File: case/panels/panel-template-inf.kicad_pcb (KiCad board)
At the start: 2 copper layers, 100 x 128.5 mm, 4 parts

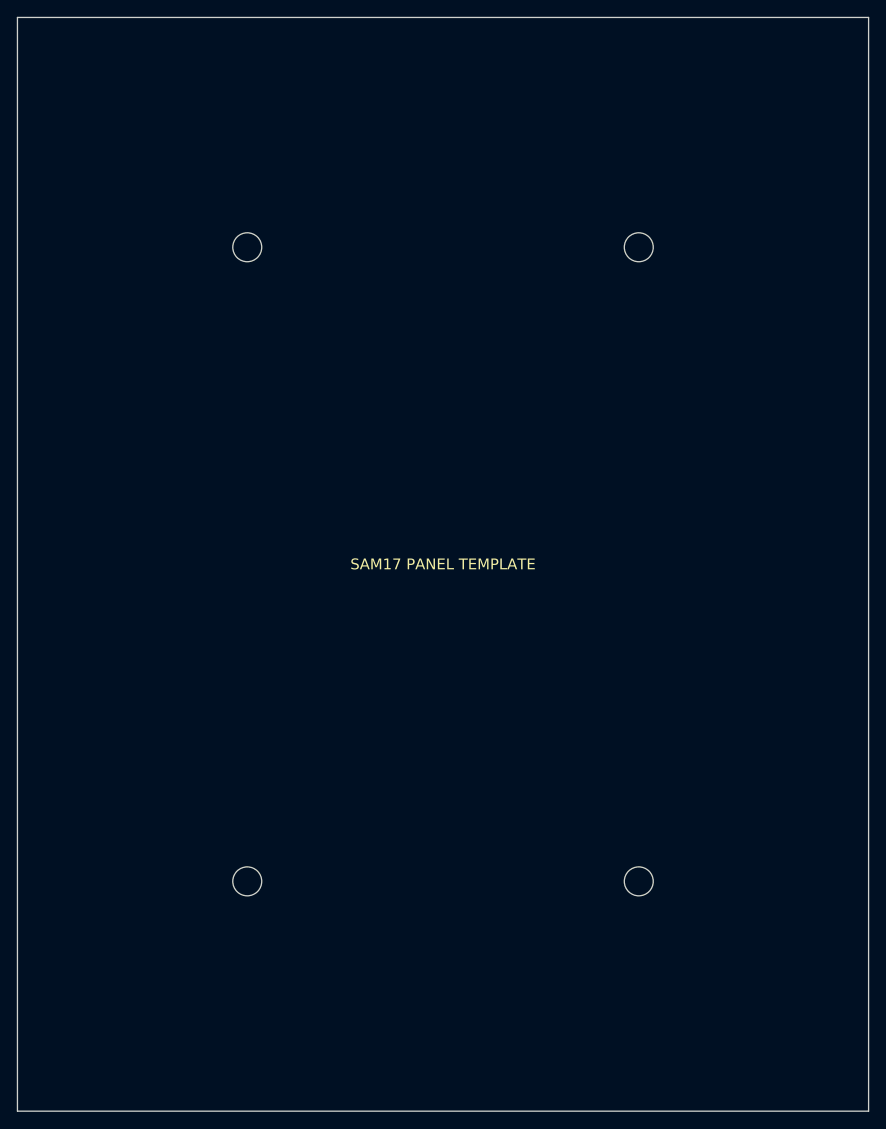
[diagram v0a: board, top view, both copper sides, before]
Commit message: Case: cara y panel dejan de ser el mismo numero, y EUROrack pasa a verde
La puerta de EUROrack estaba roja porque `alto_panel_inf` hacia dos trabajos
a la vez: era el tramo del perfil del costado Y el alto de la PCB. Con los
dos valiendo 128.5 y los railes a inset 27 de cada punta, los railes
quedaban a 74.5 mm y un modulo 3U no atornillaba.

Se separan:

  alto_cara_*   el tramo del perfil. Dibuja la silueta y sujeta los railes.
  alto_panel_*  la PCB de aluminio. Es lo unico que ve el fabricante.

En el piso de arriba coinciden (el panel cubre la cara entera; hay un assert
que lo exige). En el de abajo ya no pueden, y la cara se dimensiona DESDE el
estandar en vez de al reves:

  alto_cara_inf = sep_railes_inf + inset_tornillo + inset_valle
                = 122.5 + 27 + 15 = 164.5

Los dos insets de esa cara son asimetricos a proposito. Por delante la punta
redondeada vacia alto_frontal/2 = 15 mm de acrilico, asi que el riel no puede
empezar antes de 15 + rail/2 + 2 = 27. Por el valle el vertice lleva
radio_pico = 5 y su tangente mide 2.60, asi que con 15 basta. Forzar la
simetria costaba 12 mm de altura de piso justo en el sitio que Samuel pidio
recortar ("bajar la posicion donde esta el acrilico del medio").

El precio, que es el que anunciaba el mensaje rojo viejo: el case sube.
Alto 269.6 -> 299.1, valle 135.2 -> 164.8, fondo 310.1 -> 332.1. Un 3U de
verdad son 128.5 de panel MAS el acrilico que sujeta los rieles; no hay
version corta de eso.

ASUMIDO (decision de Samuel: simular con el estandar y adaptar cuando
conteste SynthRacks): que el riel EUROrack real se atornille sobre el 2020
con su linea roscada en la centerline del perfil. Si viene descentrada, lo
unico que se mueve es inset_valle y con el alto_cara_inf -- la silueta se
readapta sin tocar nada mas.

De paso, dos fallos que salian de la misma confusion:

  * build_template.py habria generado el panel del piso inferior de 164.5 mm
    de alto (la CARA) en vez de 128.5 (la PCB), y sin que nada avisar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
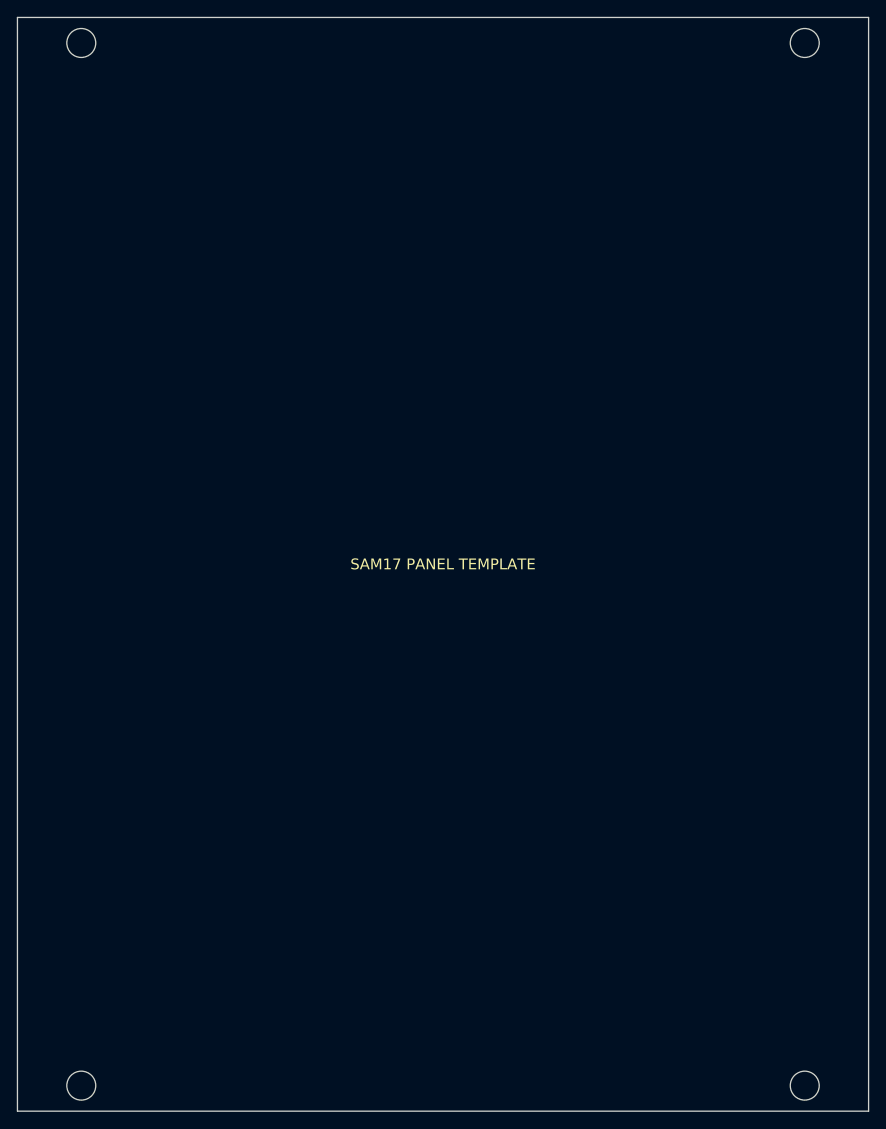
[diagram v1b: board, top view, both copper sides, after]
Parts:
- removed the ? at (27.0, 101.5)
- removed the ? at (73.0, 27.0)
- removed the ? at (73.0, 101.5)
- removed the ? at (27.0, 27.0)
- added ?: , , F.Cu at (92.5, 3.00)
- added ?: , , F.Cu at (7.50, 125.5)
- added ?: , , F.Cu at (7.50, 3.00)
- added ?: , , F.Cu at (92.5, 125.5)
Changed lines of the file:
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@@
 	(footprint ""
 		(layer "F.Cu")
-		(at 27 101.5)
+		(at 92.5 3)
 		(property "Reference" ""
 			(at 0 0 0)
@@
 	(footprint ""
 		(layer "F.Cu")
-		(at 73 27)
+		(at 7.5 125.5)
 		(property "Reference" ""
 			(at 0 0 0)
@@
 	(footprint ""
 		(layer "F.Cu")
-		(at 73 101.5)
+		(at 7.5 3)
 		(property "Reference" ""
 			(at 0 0 0)
@@
 	(footprint ""
 		(layer "F.Cu")
-		(at 27 27)
+		(at 92.5 125.5)
 		(property "Reference" ""
 			(at 0 0 0)

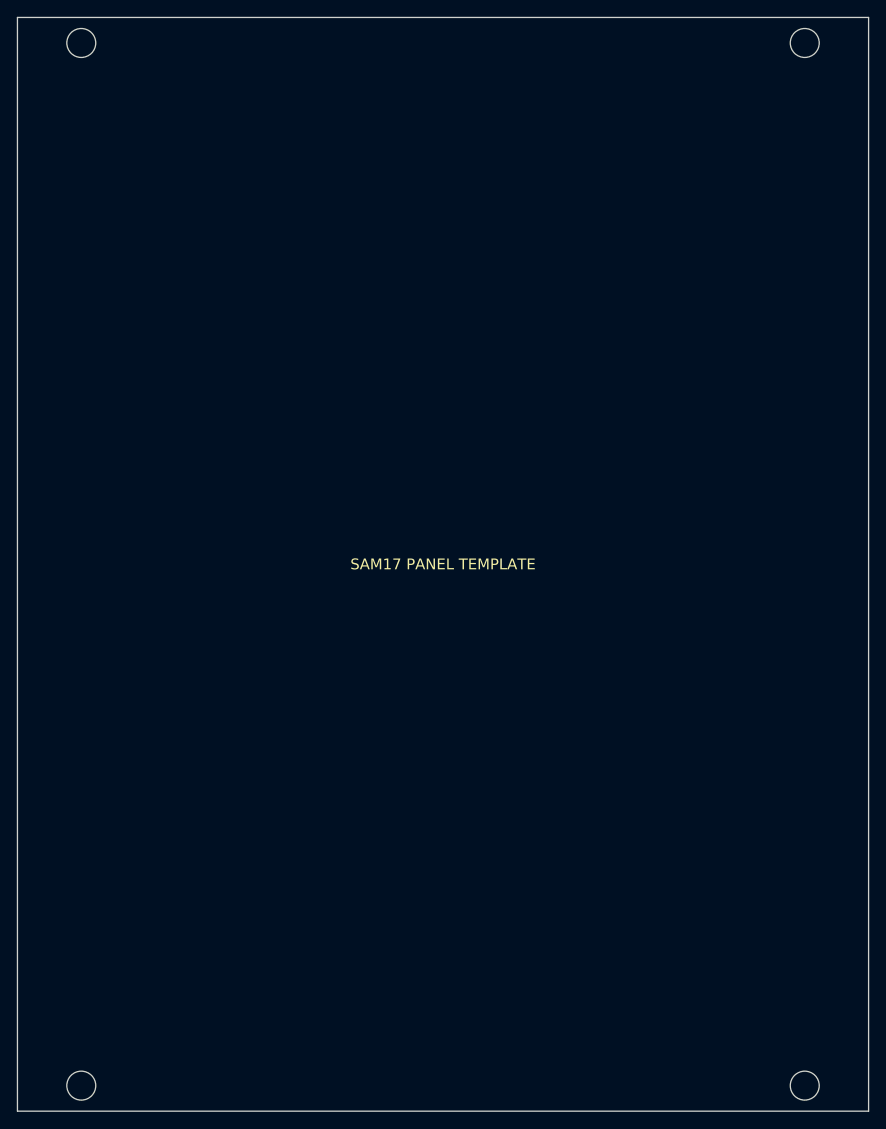
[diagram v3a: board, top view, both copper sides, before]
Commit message: Case: entra el riel EUROrack REAL; se acabo el supuesto que sostenia la silueta
Contesto StudioRacks (John, 2026-08-17) con dos planos y la cota que faltaba.
Todo lo que estaba marcado ASUMIDO en params.scad se cambia por medido.

QUE DICEN LOS PLANOS

  Riel     seccion 27.40 (fondo, hacia dentro) x 10.00 (alto, a lo largo del
           panel). Taladro de 4.5 para el M5 de punta a 13.70 de cada canto en
           fondo y 5.00 en alto: cae en el centroide.
  Mejilla  FLAT-S 133.00 x 30.50, dos M5 a 5.00 de cada punta -> 123.00 ENTRE
           CENTROS, eje a 13.80 del canto delantero. Los dos planos se
           confirman: 13.70 del riel contra 13.80 de la mejilla.

LOS DOS SUPUESTOS QUE CAEN

1. NO HAY 2020 DETRAS DE LAS CARAS. Se suponia que el riel EUROrack iria
   atornillado encima de un 2020; el plano ensena que se fija de punta con un
   M5 directo al acrilico. Los 2020 se quedan solo en el esqueleto, que es
   donde hacen estructura. El costado sigue con sus mismos taladros: lo que
   cambia es que ahora entran al riel y no a un perfil intermedio.

2. LA SEPARACION NO ES 122.50 SINO 123.00. Doepfer es el estandar de catalogo;
   el riel que se compra es el que atornilla. De ahi inset_er = 2.75 y no 3.0,
   que es la resta (128.5 - 123)/2 y no una eleccion.

   Consecuencia que hay que saber y queda escrita: un modulo de terceros con
   sus taladros a 3.0 queda 0.25 mm descentrado por lado. En taladro de 3.2
   sobre M3 hay 0.2 de juego radial, o sea que entra pero justo.

LO QUE MUEVE EN LA GEOMETRIA

  rail_er_alto/fondo/eje   nuevos: 10 / 27.4 / 13.7
  sep_railes_inf y sup     122.5 -> 123.0
  inset_er                 3.0   -> 2.75
  inset_inf_frente         26.5  -> 23.5
  inset_inf_valle          15    -> 10
  inset_sup_valle          24.5  -> 19.5
  inset_sup_remate         16    -> 15.75
  alto_frontal             28    -> 31
  alto_cara_inf            164.0 -> 156.5
  alto_cara_sup            163.0 -> 158.25

  alto   277.6 -> 271.1      fondo  298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
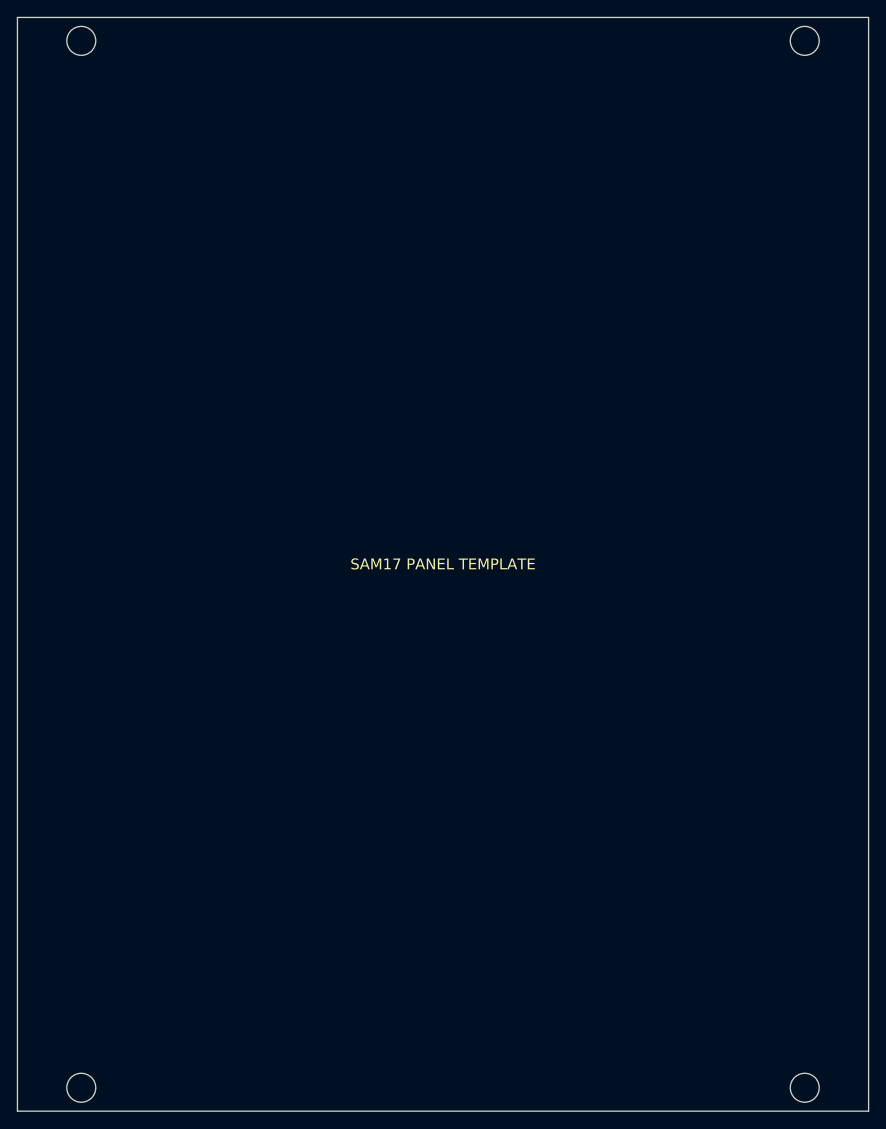
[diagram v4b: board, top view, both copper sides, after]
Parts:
- removed the ? at (7.50, 125.5)
- removed the ? at (92.5, 3.00)
- removed the ? at (92.5, 125.5)
- removed the ? at (7.50, 3.00)
- added ?: , , F.Cu at (92.5, 2.75)
- added ?: , , F.Cu at (7.50, 2.75)
- added ?: , , F.Cu at (92.5, 125.8)
- added ?: , , F.Cu at (7.50, 125.8)
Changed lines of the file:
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@@
 	(footprint ""
 		(layer "F.Cu")
-		(at 7.5 125.5)
+		(at 92.5 2.75)
 		(property "Reference" ""
 			(at 0 0 0)
@@
 	(footprint ""
 		(layer "F.Cu")
-		(at 92.5 3)
+		(at 7.5 2.75)
 		(property "Reference" ""
 			(at 0 0 0)
@@
 	(footprint ""
 		(layer "F.Cu")
-		(at 92.5 125.5)
+		(at 92.5 125.75)
 		(property "Reference" ""
 			(at 0 0 0)
@@
 	(footprint ""
 		(layer "F.Cu")
-		(at 7.5 3)
+		(at 7.5 125.75)
 		(property "Reference" ""
 			(at 0 0 0)
